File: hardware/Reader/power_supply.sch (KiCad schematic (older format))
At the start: 3 parts

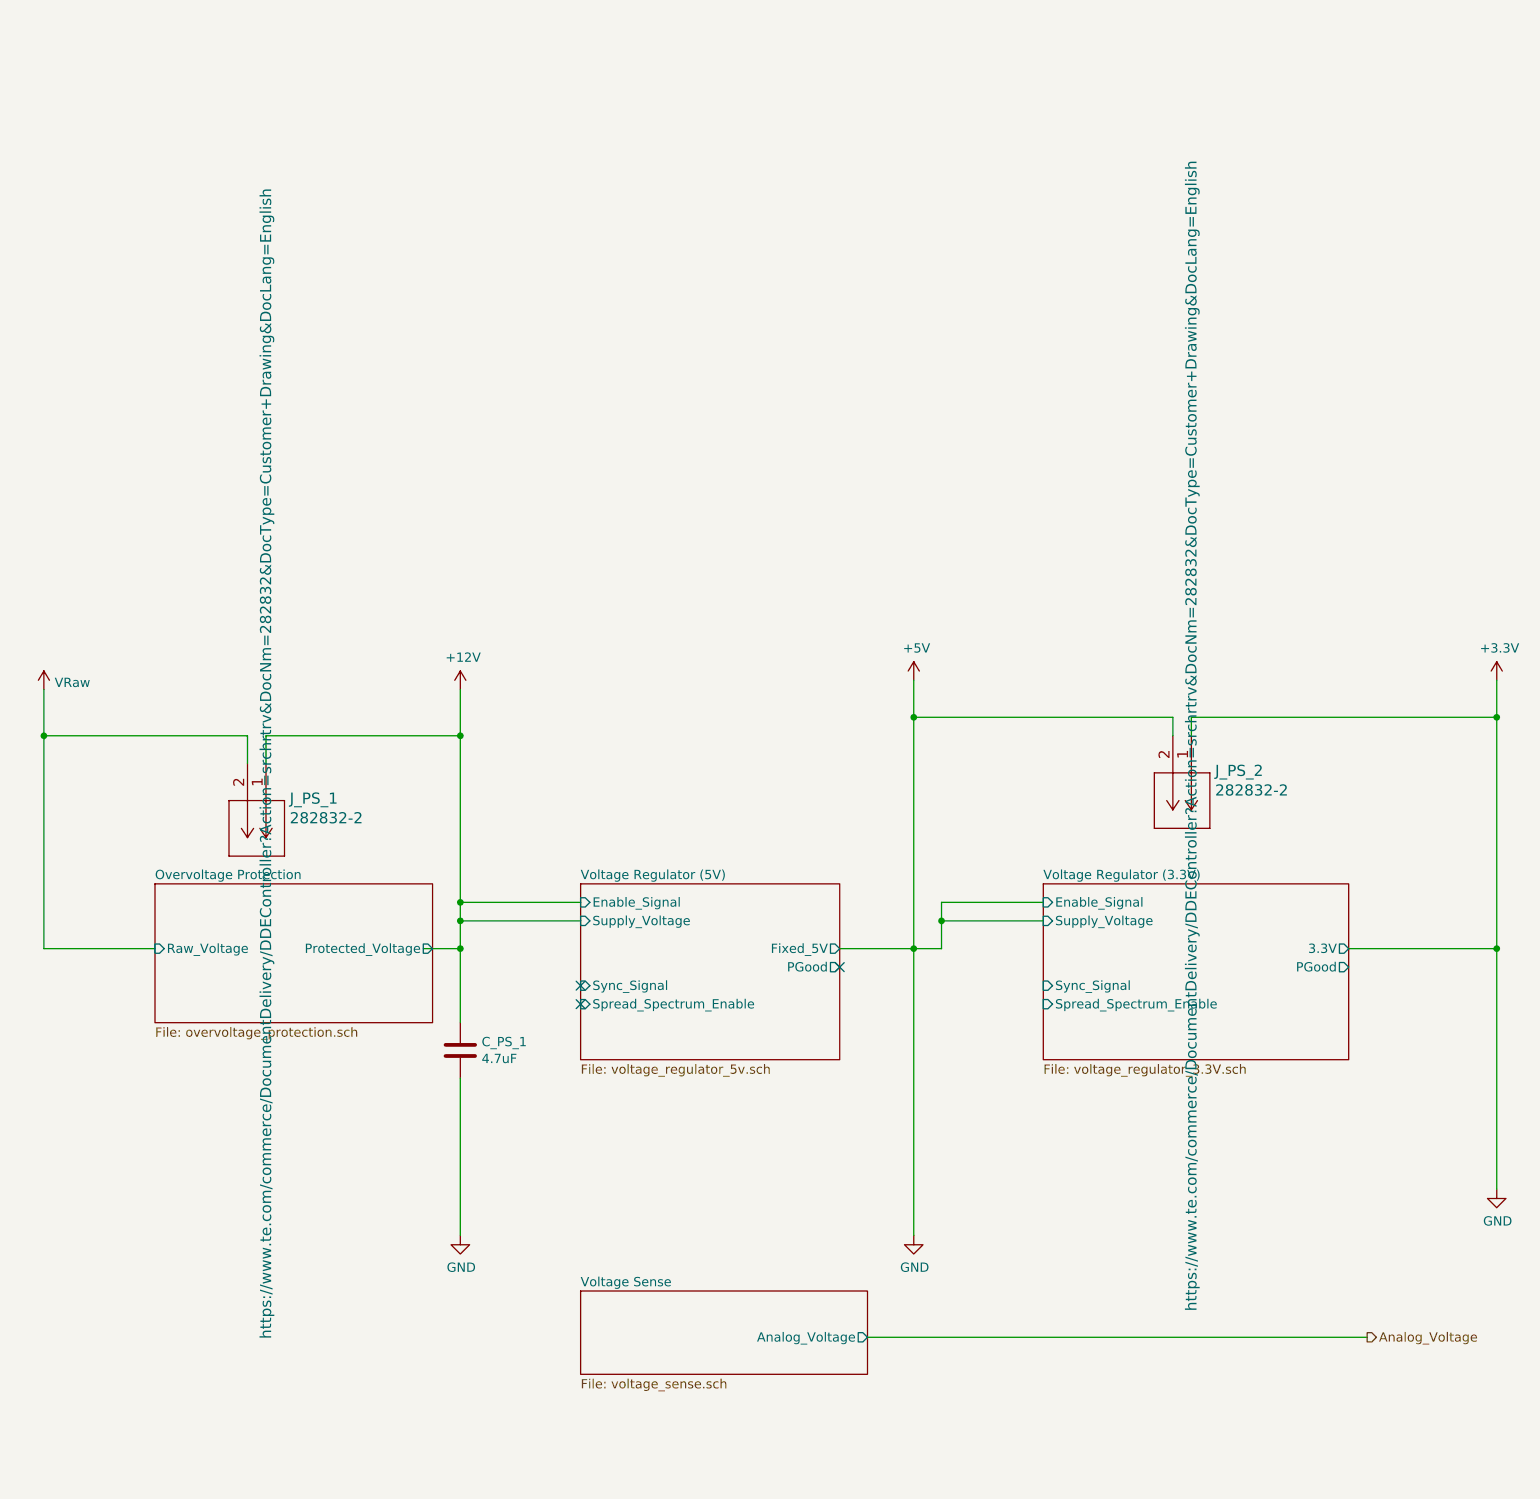
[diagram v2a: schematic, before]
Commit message: Minor changes to schematic design for clarity. Added important IC datasheets. Exported schematics and rough gerber files
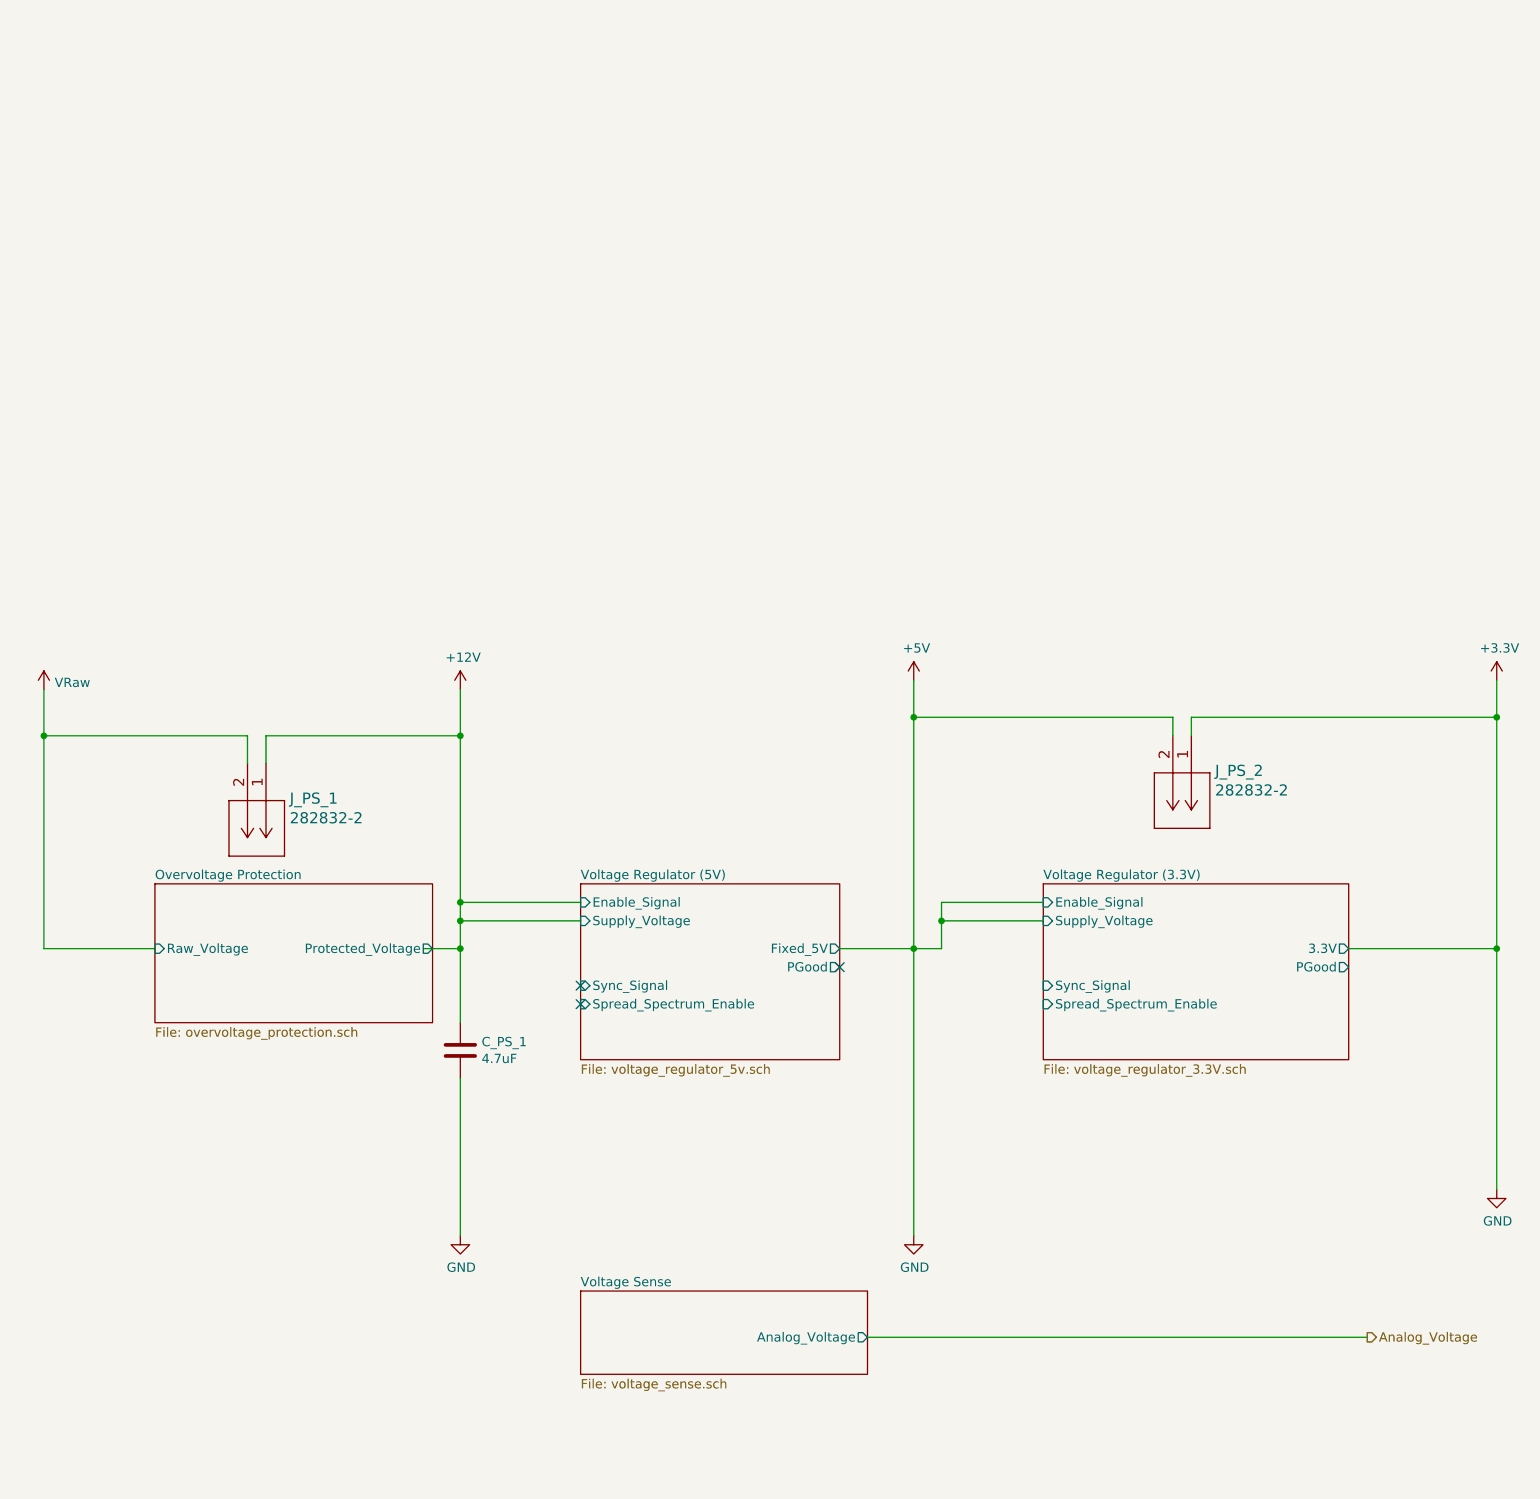
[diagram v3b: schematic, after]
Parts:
- J_PS_1, J_PS_2: Part Number 282832-2 -> (none)
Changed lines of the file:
@@
 F 1 "282832-2" V 2595 1928 60  0000 L CNN
 F 2 "footprints:282832-2" H 2700 1740 60  0001 C CNN
-F 3 "https://www.te.com/commerce/DocumentDelivery/DDEController?Action=srchrtrv&DocNm=282832&DocType=Customer+Drawing&DocLang=English" H 2300 1800 60  0000 C CNN
-F 4 "282832-2" V 2300 1800 50  0001 C CNN "Part Number"
-F 5 "282832-2" H 2300 1800 50  0001 C CNN "Part Name"
+F 3 "https://www.te.com/commerce/DocumentDelivery/DDEController?Action=srchrtrv&DocNm=282832&DocType=Customer+Drawing&DocLang=English" H 2300 1800 60  0001 C CNN
+F 4 "282832-2" H 2300 1800 50  0001 C CNN "Part Name"
 	1    2300 1800
 	0    1    1    0
@@
 F 1 "282832-2" V 7595 1778 60  0000 L CNN
 F 2 "footprints:282832-2" H 7700 1590 60  0001 C CNN
-F 3 "https://www.te.com/commerce/DocumentDelivery/DDEController?Action=srchrtrv&DocNm=282832&DocType=Customer+Drawing&DocLang=English" H 7300 1650 60  0000 C CNN
-F 4 "282832-2" V 7300 1650 50  0001 C CNN "Part Number"
-F 5 "282832-2" H 7300 1650 50  0001 C CNN "Part Name"
+F 3 "https://www.te.com/commerce/DocumentDelivery/DDEController?Action=srchrtrv&DocNm=282832&DocType=Customer+Drawing&DocLang=English" H 7300 1650 60  0001 C CNN
+F 4 "282832-2" H 7300 1650 50  0001 C CNN "Part Name"
 	1    7300 1650
 	0    1    1    0

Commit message: Added ESD Protection. Fixed minor bugs on schematic. Attempted placement of components
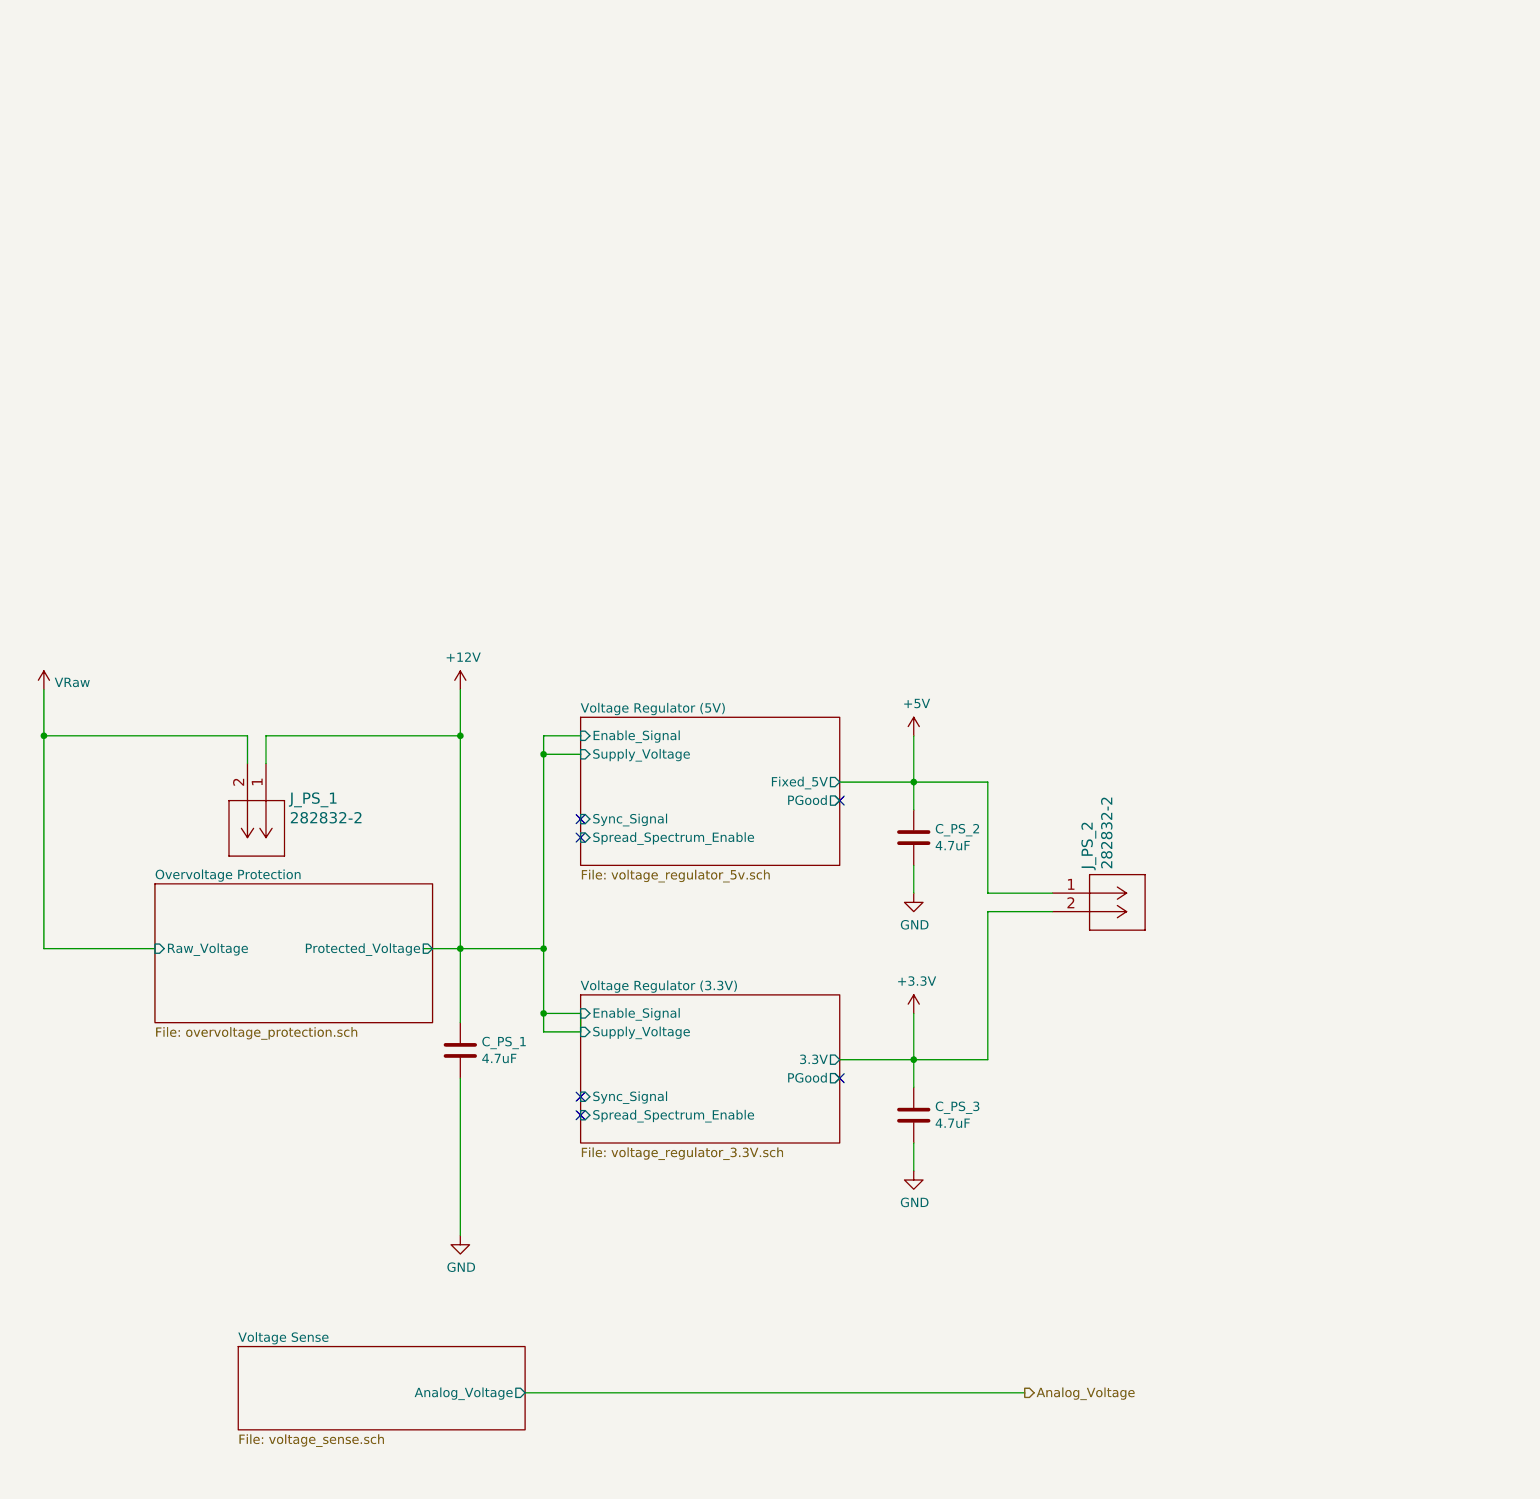
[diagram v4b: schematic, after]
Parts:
- added C_PS_2, C_PS_3: 4.7uF, footprints:C1206C475K3RACAUTO, symbol Device:C
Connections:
- wire segments 34 -> 37
- no-connect marks 3 -> 6
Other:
- moved on the sheet: J_PS_2

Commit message: Fixed bugs on the reader schematic. Exported Schematic Electrical report
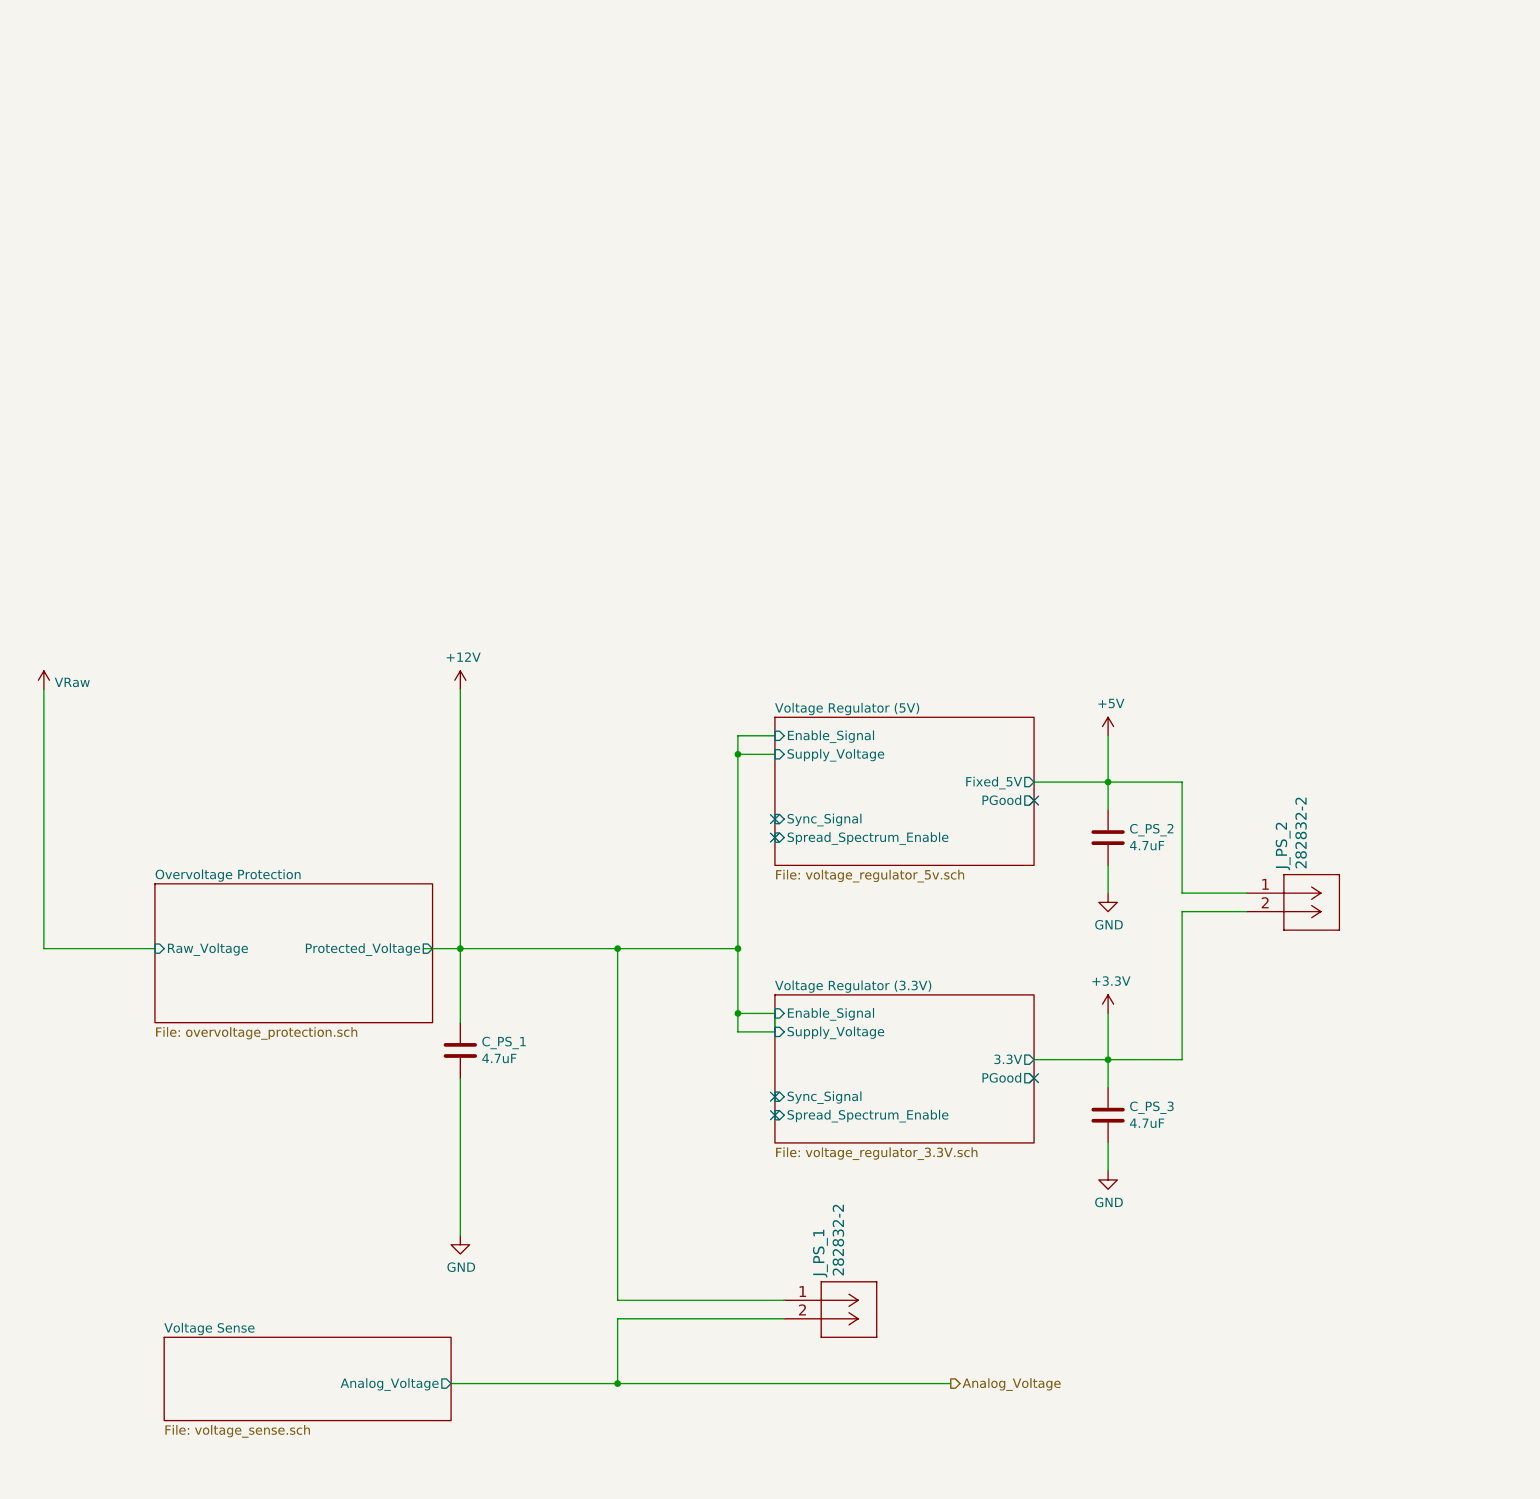
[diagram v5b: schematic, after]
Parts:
- C_PS_1, C_PS_2, C_PS_3: Manufacturer (none) -> Kermet; Vendor (none) -> DigiKey Canada; digikeypn (none) -> 399-7029-1-ND
- J_PS_1, J_PS_2: Manufacturer (none) -> TE Connectivity AMP Connectors; Vendor (none) -> DigiKey Canada; digikeypn (none) -> A113314-ND
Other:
- moved on the sheet: C_PS_2, C_PS_3, J_PS_1, J_PS_2
